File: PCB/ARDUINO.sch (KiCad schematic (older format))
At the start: 16 parts, among them J1 ICSP, J2 FTDI, SW1 RESET, U1 ATMEGA328P_TQFP, Y1 16MHz

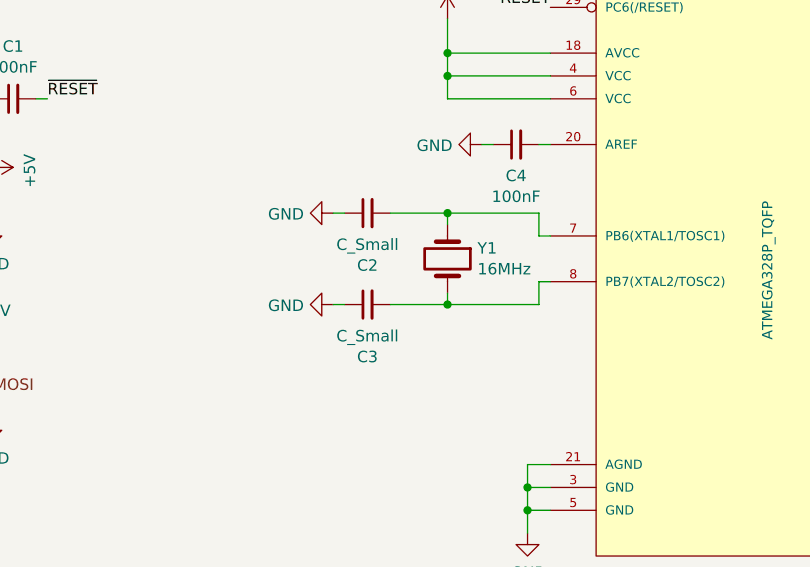
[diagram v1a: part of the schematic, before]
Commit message: Swapped crystal for resonator
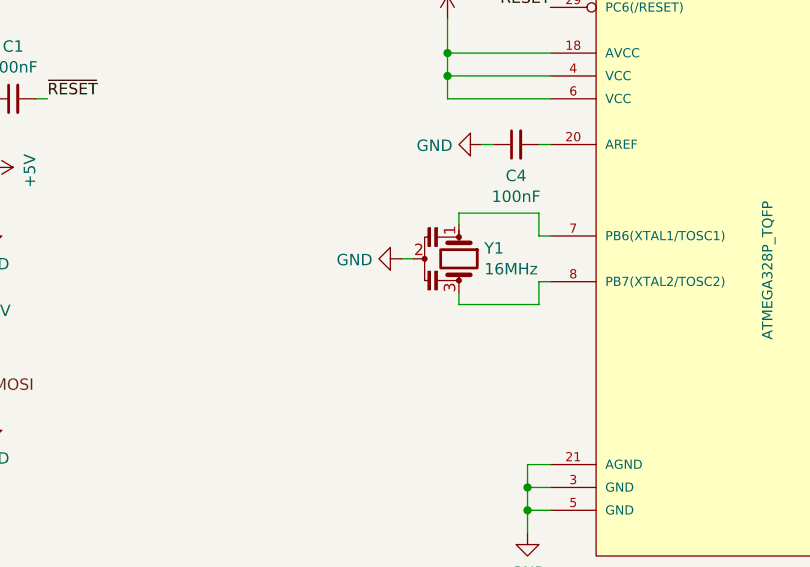
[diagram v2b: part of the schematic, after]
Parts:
- removed C2, C3: C_Small, symbol Device:C_Small
- removed Y1: 16MHz, symbol Device:Crystal
- added Y1: 16MHz, symbol Device:Resonator
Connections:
- net GND: now also Y1.2
- net at U1.7 (PB6(XTAL1/TOSC1)): now also Y1.1
- net at U1.8 (PB7(XTAL2/TOSC2)): now also Y1.3
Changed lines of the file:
@@
 $EndComp
-$Comp
-L Device:Crystal Y?
-U 1 1 5E88BF03
-P 4450 3950
-AR Path="/5E88BF03" Ref="Y?"  Part="1"
-AR Path="/5E880AC6/5E88BF03" Ref="Y1"  Part="1"
-F 0 "Y1" V 4404 4081 50  0000 L CNN
-F 1 "16MHz" V 4495 4081 50  0000 L CNN
-F 2 "" H 4450 3950 50  0001 C CNN
-F 3 "" H 4450 3950 50  0001 C CNN
-	1    4450 3950
-	0    1    1    0
-$EndComp
-$Comp
-L Device:C_Small C?
-U 1 1 5E88BF09
-P 4100 4150
-AR Path="/5E88BF09" Ref="C?"  Part="1"
-AR Path="/5E880AC6/5E88BF09" Ref="C3"  Part="1"
-F 0 "C3" V 3871 4150 50  0000 C CNN
-F 1 "C_Small" V 3962 4150 50  0000 C CNN
-F 2 "" H 4100 4150 50  0001 C CNN
-F 3 "" H 4100 4150 50  0001 C CNN
-F 4 "C0G" H 4100 4150 50  0001 C CNN "Dielectric"
-F 5 "6.3V" H 4100 4150 50  0001 C CNN "Voltage Rating"
-	1    4100 4150
-	0    -1   -1   0
-$EndComp
-$Comp
-L Device:C_Small C?
-U 1 1 5E88BF0F
-P 4100 3750
-AR Path="/5E88BF0F" Ref="C?"  Part="1"
-AR Path="/5E880AC6/5E88BF0F" Ref="C2"  Part="1"
-F 0 "C2" V 3871 3750 50  0000 C CNN
-F 1 "C_Small" V 3962 3750 50  0000 C CNN
-F 2 "" H 4100 3750 50  0001 C CNN
-F 3 "" H 4100 3750 50  0001 C CNN
-F 4 "C0G" H 4100 3750 50  0001 C CNN "Dielectric"
-F 5 "6.3V" H 4100 3750 50  0001 C CNN "Voltage Rating"
-	1    4100 3750
-	0    -1   -1   0
-$EndComp
-Wire Wire Line
-	4200 4150 4450 4150
-Wire Wire Line
-	4450 4150 4450 4100
-Wire Wire Line
-	4450 4150 4850 4150
-Wire Wire Line
-	4850 4150 4850 4050
-Connection ~ 4450 4150
-Wire Wire Line
-	4850 3850 4850 3750
-Wire Wire Line
-	4850 3750 4450 3750
-Wire Wire Line
-	4450 3800 4450 3750
-Connection ~ 4450 3750
-Wire Wire Line
-	4450 3750 4200 3750
 $Comp
 L power:GND #PWR?
 U 1 1 5E88BF1F
-P 3950 4150
+P 4250 3950
 AR Path="/5E88BF1F" Ref="#PWR?"  Part="1"
 AR Path="/5E880AC6/5E88BF1F" Ref="#PWR010"  Part="1"
-F 0 "#PWR010" H 3950 3900 50  0001 C CNN
-F 1 "GND" V 3955 4022 50  0000 R CNN
-F 2 "" H 3950 4150 50  0001 C CNN
-F 3 "" H 3950 4150 50  0001 C CNN
-	1    3950 4150
+F 0 "#PWR010" H 4250 3700 50  0001 C CNN
+F 1 "GND" V 4255 3822 50  0000 R CNN
+F 2 "" H 4250 3950 50  0001 C CNN
+F 3 "" H 4250 3950 50  0001 C CNN
+	1    4250 3950
 	0    1    1    0
 $EndComp
 Wire Wire Line
-	3950 3750 4000 3750
-Wire Wire Line
-	3950 4150 4000 4150
-$Comp
-L power:GND #PWR?
-U 1 1 5E88BF2D
-P 3950 3750
-AR Path="/5E88BF2D" Ref="#PWR?"  Part="1"
-AR Path="/5E880AC6/5E88BF2D" Ref="#PWR09"  Part="1"
-F 0 "#PWR09" H 3950 3500 50  0001 C CNN
-F 1 "GND" V 3955 3622 50  0000 R CNN
-F 2 "" H 3950 3750 50  0001 C CNN
-F 3 "" H 3950 3750 50  0001 C CNN
-	1    3950 3750
-	0    1    1    0
-$EndComp
+	4250 3950 4300 3950
 $Comp
 L power:GND #PWR?
@@
 	1    0    0    -1
 $EndComp
+$Comp
+L Device:Resonator Y1
+U 1 1 5E9074AD
+P 4500 3950
+F 0 "Y1" V 4454 4061 50  0000 L CNN
+F 1 "16MHz" V 4545 4061 50  0000 L CNN
+F 2 "" H 4475 3950 50  0001 C CNN
+F 3 "~" H 4475 3950 50  0001 C CNN
+	1    4500 3950
+	0    1    1    0
+$EndComp
+Wire Wire Line
+	4850 4050 4850 4150
+Wire Wire Line
+	4850 4150 4500 4150
+Wire Wire Line
+	4500 4150 4500 4100
+Wire Wire Line
+	4850 3850 4850 3750
+Wire Wire Line
+	4850 3750 4500 3750
+Wire Wire Line
+	4500 3750 4500 3800
 $EndSCHEMATC

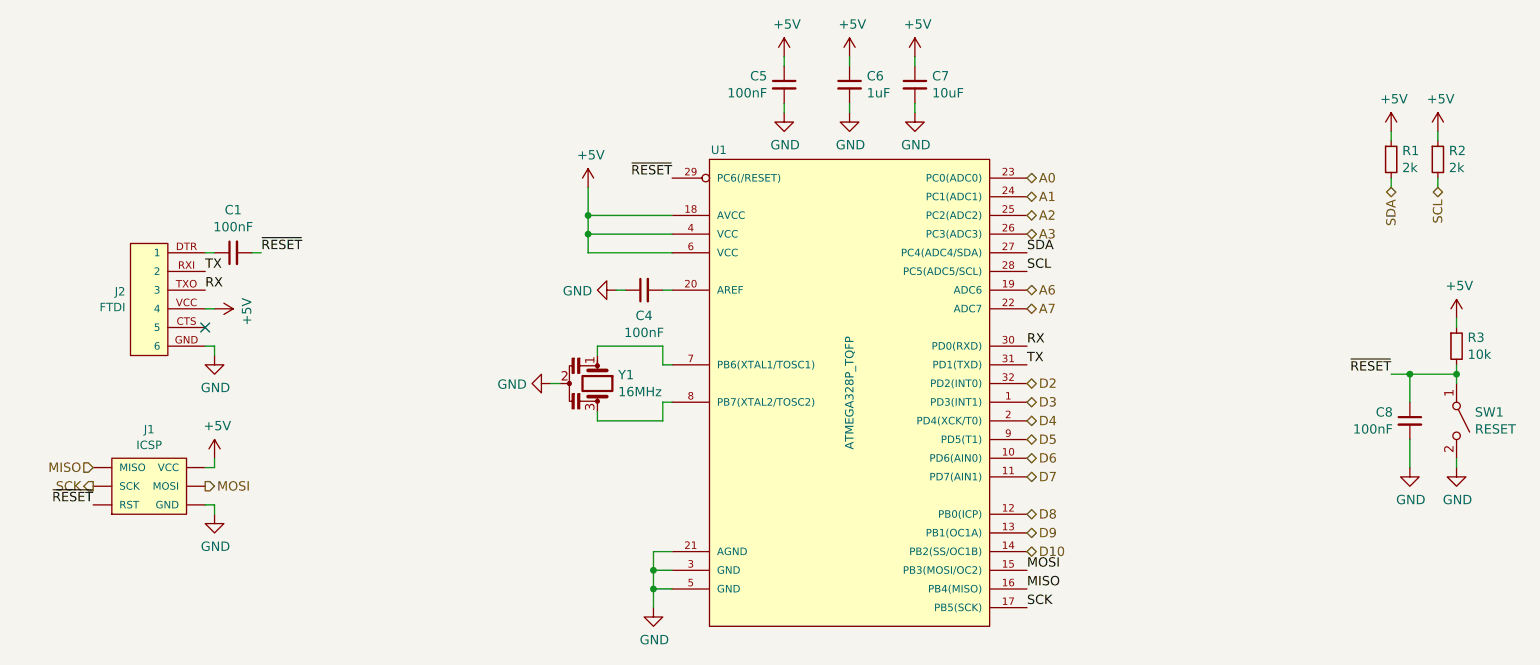
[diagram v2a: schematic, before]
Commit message: Added remaining test points
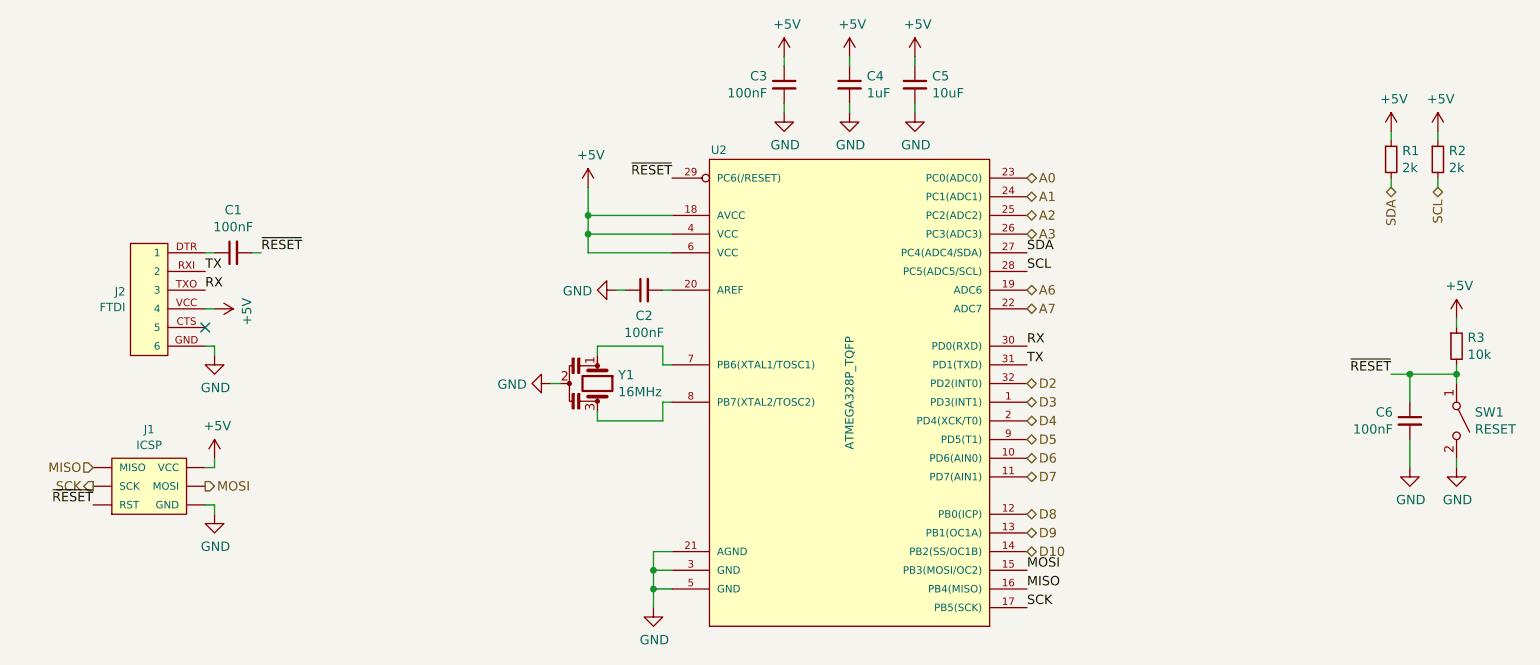
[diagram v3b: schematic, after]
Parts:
- renumbered C4 to C2, C5 to C3, C6 to C4, C7 to C5, C8 to C6, U1 to U2
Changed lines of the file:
@@
 P 5850 4000
 AR Path="/5E88BF58" Ref="U?"  Part="1"
-AR Path="/5E880AC6/5E88BF58" Ref="U1"  Part="1"
-F 0 "U1" H 5150 5300 45  0000 C CNN
+AR Path="/5E880AC6/5E88BF58" Ref="U2"  Part="1"
+F 0 "U2" H 5150 5300 45  0000 C CNN
 F 1 "ATMEGA328P_TQFP" V 5850 4000 45  0000 C CNN
 F 2 "" H 5850 5350 20  0001 C CNN
@@
 P 2450 4650
 AR Path="/5E88BF7D" Ref="#PWR?"  Part="1"
-AR Path="/5E880AC6/5E88BF7D" Ref="#PWR08"  Part="1"
-F 0 "#PWR08" H 2450 4400 50  0001 C CNN
+AR Path="/5E880AC6/5E88BF7D" Ref="#PWR09"  Part="1"
+F 0 "#PWR09" H 2450 4400 50  0001 C CNN
 F 1 "GND" H 2455 4477 50  0000 C CNN
 F 2 "" H 2450 4650 50  0001 C CNN
@@
 P 8850 4150
 AR Path="/5E88BF85" Ref="C?"  Part="1"
-AR Path="/5E880AC6/5E88BF85" Ref="C8"  Part="1"
-F 0 "C8" H 8759 4196 50  0000 R CNN
+AR Path="/5E880AC6/5E88BF85" Ref="C6"  Part="1"
+F 0 "C6" H 8759 4196 50  0000 R CNN
 F 1 "100nF" H 8759 4105 50  0000 R CNN
 F 2 "" H 8850 4150 50  0001 C CNN
@@
 P 2450 3800
 AR Path="/5E88BF98" Ref="#PWR?"  Part="1"
-AR Path="/5E880AC6/5E88BF98" Ref="#PWR06"  Part="1"
-F 0 "#PWR06" H 2450 3550 50  0001 C CNN
+AR Path="/5E880AC6/5E88BF98" Ref="#PWR07"  Part="1"
+F 0 "#PWR07" H 2450 3550 50  0001 C CNN
 F 1 "GND" H 2455 3627 50  0000 C CNN
 F 2 "" H 2450 3800 50  0001 C CNN
@@
 P 4750 3450
 AR Path="/5E88BFA7" Ref="C?"  Part="1"
-AR Path="/5E880AC6/5E88BFA7" Ref="C4"  Part="1"
-F 0 "C4" V 4613 3450 50  0000 C CNN
+AR Path="/5E880AC6/5E88BFA7" Ref="C2"  Part="1"
+F 0 "C2" V 4613 3450 50  0000 C CNN
 F 1 "100nF" V 4522 3450 50  0000 C CNN
 F 2 "" H 4750 3450 50  0001 C CNN
@@
 P 5500 2350
 AR Path="/5E88BFE3" Ref="C?"  Part="1"
-AR Path="/5E880AC6/5E88BFE3" Ref="C5"  Part="1"
-F 0 "C5" H 5409 2396 50  0000 R CNN
+AR Path="/5E880AC6/5E88BFE3" Ref="C3"  Part="1"
+F 0 "C3" H 5409 2396 50  0000 R CNN
 F 1 "100nF" H 5409 2305 50  0000 R CNN
 F 2 "" H 5500 2350 50  0001 C CNN
@@
 P 5850 2350
 AR Path="/5E88BFE9" Ref="C?"  Part="1"
-AR Path="/5E880AC6/5E88BFE9" Ref="C6"  Part="1"
-F 0 "C6" H 5942 2396 50  0000 L CNN
+AR Path="/5E880AC6/5E88BFE9" Ref="C4"  Part="1"
+F 0 "C4" H 5942 2396 50  0000 L CNN
 F 1 "1uF" H 5942 2305 50  0000 L CNN
 F 2 "" H 5850 2350 50  0001 C CNN
@@
 P 6200 2350
 AR Path="/5E88BFEF" Ref="C?"  Part="1"
-AR Path="/5E880AC6/5E88BFEF" Ref="C7"  Part="1"
-F 0 "C7" H 6292 2396 50  0000 L CNN
+AR Path="/5E880AC6/5E88BFEF" Ref="C5"  Part="1"
+F 0 "C5" H 6292 2396 50  0000 L CNN
 F 1 "10uF" H 6292 2305 50  0000 L CNN
 F 2 "" H 6200 2350 50  0001 C CNN
@@
 P 2450 4350
 AR Path="/5E8A6686/5E90F2A1" Ref="#PWR?"  Part="1"
-AR Path="/5E880AC6/5E90F2A1" Ref="#PWR07"  Part="1"
-F 0 "#PWR07" H 2450 4200 50  0001 C CNN
+AR Path="/5E880AC6/5E90F2A1" Ref="#PWR08"  Part="1"
+F 0 "#PWR08" H 2450 4200 50  0001 C CNN
 F 1 "+5V" H 2465 4523 50  0000 C CNN
 F 2 "" H 2450 4350 50  0001 C CNN
@@
 P 2450 3550
 AR Path="/5E8A6686/5E910278" Ref="#PWR?"  Part="1"
-AR Path="/5E880AC6/5E910278" Ref="#PWR05"  Part="1"
-F 0 "#PWR05" H 2450 3400 50  0001 C CNN
+AR Path="/5E880AC6/5E910278" Ref="#PWR06"  Part="1"
+F 0 "#PWR06" H 2450 3400 50  0001 C CNN
 F 1 "+5V" H 2465 3723 50  0000 C CNN
 F 2 "" H 2450 3550 50  0001 C CNN

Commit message: Swapped MSx jumpers around so that fullstep is default
The footprint used defaults to bridging pins 2 and 3
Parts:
- J1: footprint (none) -> Connector_PinHeader_2.54mm:PinHeader_2x03_P2.54mm_Vertical_SMD
- J2: footprint (none) -> Connectors:FTDI_BASIC
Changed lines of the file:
@@
 F 0 "J2" H 1973 3458 45  0000 R CNN
 F 1 "FTDI" H 1973 3542 45  0000 R CNN
-F 2 "" H 2200 3950 20  0001 C CNN
+F 2 "Connectors:FTDI_BASIC" H 2200 3950 20  0001 C CNN
 F 3 "" H 2200 3250 50  0001 C CNN
 	1    2200 3250
@@
 F 0 "J1" H 2100 4804 45  0000 C CNN
 F 1 "ICSP" H 2100 4720 45  0000 C CNN
-F 2 "" H 2100 4800 20  0001 C CNN
+F 2 "Connector_PinHeader_2.54mm:PinHeader_2x03_P2.54mm_Vertical_SMD" H 2100 4800 20  0001 C CNN
 F 3 "" H 2100 4500 50  0001 C CNN
 	1    2100 4500

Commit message: Added majority footprints
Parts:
- C1, C2, C3, C4, C5, C6: footprint (none) -> Capacitor_SMD:C_0603_1608Metric
- R1, R2, R3: footprint (none) -> Resistor_SMD:R_0603_1608Metric
- SW1: footprint (none) -> Switches:TACTILE_SWITCH_SMD_5.2MM
- U2: footprint (none) -> Package_QFP:TQFP-32_7x7mm_P0.8mm
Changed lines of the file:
@@
 AR Path="/5E88BF39" Ref="SW?"  Part="1"
 AR Path="/5E880AC6/5E88BF39" Ref="SW1"  Part="1"
+AR Path="/5E86C5C8/5E88BF39" Ref="SW1"  Part="1"
 F 0 "SW1" V 9054 4248 50  0000 L CNN
 F 1 "RESET" V 9145 4248 50  0000 L CNN
-F 2 "" H 9100 4150 50  0001 C CNN
+F 2 "Switches:TACTILE_SWITCH_SMD_5.2MM" H 9100 4150 50  0001 C CNN
 F 3 "" H 9100 4150 50  0001 C CNN
 	1    9100 4150
@@
 F 0 "R3" H 9159 3796 50  0000 L CNN
 F 1 "10k" H 9159 3705 50  0000 L CNN
-F 2 "" H 9100 3750 50  0001 C CNN
+F 2 "Resistor_SMD:R_0603_1608Metric" H 9100 3750 50  0001 C CNN
 F 3 "" H 9100 3750 50  0001 C CNN
 	1    9100 3750
@@
 F 0 "U2" H 5150 5300 45  0000 C CNN
 F 1 "ATMEGA328P_TQFP" V 5850 4000 45  0000 C CNN
-F 2 "" H 5850 5350 20  0001 C CNN
+F 2 "Package_QFP:TQFP-32_7x7mm_P0.8mm" H 5850 5350 20  0001 C CNN
 F 3 "http://ww1.microchip.com/downloads/en/DeviceDoc/Atmel-7810-Automotive-Microcontrollers-ATmega328P_Datasheet.pdf" H 5850 4000 50  0001 C CNN
 	1    5850 4000
@@
 F 0 "C6" H 8759 4196 50  0000 R CNN
 F 1 "100nF" H 8759 4105 50  0000 R CNN
-F 2 "" H 8850 4150 50  0001 C CNN
+F 2 "Capacitor_SMD:C_0603_1608Metric" H 8850 4150 50  0001 C CNN
 F 3 "" H 8850 4150 50  0001 C CNN
 F 4 "X7R" H 8850 4150 50  0001 C CNN "Dielectric"
@@
 F 0 "C2" V 4613 3450 50  0000 C CNN
 F 1 "100nF" V 4522 3450 50  0000 C CNN
-F 2 "" H 4750 3450 50  0001 C CNN
+F 2 "Capacitor_SMD:C_0603_1608Metric" H 4750 3450 50  0001 C CNN
 F 3 "" H 4750 3450 50  0001 C CNN
 F 4 "X7R" H 4750 3450 50  0001 C CNN "Dielectric"
@@
 F 0 "C1" V 2779 3250 50  0000 C CNN
 F 1 "100nF" V 2688 3250 50  0000 C CNN
-F 2 "" H 2550 3250 50  0001 C CNN
+F 2 "Capacitor_SMD:C_0603_1608Metric" H 2550 3250 50  0001 C CNN
 F 3 "" H 2550 3250 50  0001 C CNN
 F 4 "X7R" H 2550 3250 50  0001 C CNN "Dielectric"
@@
 F 0 "R1" H 8809 2796 50  0000 L CNN
 F 1 "2k" H 8809 2705 50  0000 L CNN
-F 2 "" H 8750 2750 50  0001 C CNN
+F 2 "Resistor_SMD:R_0603_1608Metric" H 8750 2750 50  0001 C CNN
 F 3 "" H 8750 2750 50  0001 C CNN
 	1    8750 2750
@@
 F 0 "R2" H 9059 2796 50  0000 L CNN
 F 1 "2k" H 9059 2705 50  0000 L CNN
-F 2 "" H 9000 2750 50  0001 C CNN
+F 2 "Resistor_SMD:R_0603_1608Metric" H 9000 2750 50  0001 C CNN
 F 3 "" H 9000 2750 50  0001 C CNN
 	1    9000 2750
@@
 F 0 "C3" H 5409 2396 50  0000 R CNN
 F 1 "100nF" H 5409 2305 50  0000 R CNN
-F 2 "" H 5500 2350 50  0001 C CNN
+F 2 "Capacitor_SMD:C_0603_1608Metric" H 5500 2350 50  0001 C CNN
 F 3 "" H 5500 2350 50  0001 C CNN
 F 4 "X7R" H 5500 2350 50  0001 C CNN "Dielectric"
@@
 F 0 "C4" H 5942 2396 50  0000 L CNN
 F 1 "1uF" H 5942 2305 50  0000 L CNN
-F 2 "" H 5850 2350 50  0001 C CNN
+F 2 "Capacitor_SMD:C_0603_1608Metric" H 5850 2350 50  0001 C CNN
 F 3 "" H 5850 2350 50  0001 C CNN
 F 4 "X7R" H 5850 2350 50  0001 C CNN "Dielectric"
@@
 F 0 "C5" H 6292 2396 50  0000 L CNN
 F 1 "10uF" H 6292 2305 50  0000 L CNN
-F 2 "" H 6200 2350 50  0001 C CNN
+F 2 "Capacitor_SMD:C_0603_1608Metric" H 6200 2350 50  0001 C CNN
 F 3 "" H 6200 2350 50  0001 C CNN
 F 4 "X7R" H 6200 2350 50  0001 C CNN "Dielectric"

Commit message: Added more footprints
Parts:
- Y1: footprint (none) -> Crystal:Resonator_SMD_muRata_CSTxExxV-3Pin_3.0x1.1mm; MPN (none) -> CSTNE16M0V53C000R0
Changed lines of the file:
@@
 F 0 "Y1" V 4454 4061 50  0000 L CNN
 F 1 "16MHz" V 4545 4061 50  0000 L CNN
-F 2 "" H 4475 3950 50  0001 C CNN
-F 3 "~" H 4475 3950 50  0001 C CNN
+F 2 "Crystal:Resonator_SMD_muRata_CSTxExxV-3Pin_3.0x1.1mm" H 4475 3950 50  0001 C CNN
+F 3 "https://www.murata.com/en/products/productdata/8801162166302/SPEC-CSTNE16M0V53C000R0.pdf" H 4475 3950 50  0001 C CNN
+F 4 "CSTNE16M0V53C000R0" V 4500 3950 50  0001 C CNN "MPN"
 	1    4500 3950
 	0    1    1    0
